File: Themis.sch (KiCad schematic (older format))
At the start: 37 parts, among them J10 Conn_01x01, J11 Conn_01x01, J12 Conn_01x01, J13 Conn_01x01, J17 SMA, J18 Conn_01x01, J20 Conn_01x01, J5 Conn_01x05, J7 SMA, J8 SMA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

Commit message: preparing themis v2
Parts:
- D5, D6: renamed from D?; footprint (none) -> Diode_SMD:D_SMB_Handsoldering
- J17, J8: footprint SMA_PINS:SMA_EDGE_NRW -> SMA_PINS:SMA_PINS
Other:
- note added: "V2.0\n\n\n\n28B0570-000\n28B0562-100\nlaird"
- note added: "att 30dB or less\ndepending on your \noutput p0wa\n"
- note removed: "28B0562-100\nlaird"
- note removed: "att 30dB\n"
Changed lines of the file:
@@
 	6100 3800 6150 3800
 Connection ~ 6150 3800
-Text Notes 3700 3650 0    60   ~ 0
-att 30dB\n
+Text Notes 3650 3550 0    60   ~ 0
+att 30dB or less\ndepending on your \noutput p0wa\n
 $Comp
 L D_Small_ALT D1
@@
 $EndComp
 $Comp
-L GND #PWR023
+L GND #PWR022
 U 1 1 5A4D7C62
 P 5450 1350
-F 0 "#PWR023" H 5450 1100 50  0001 C CNN
+F 0 "#PWR022" H 5450 1100 50  0001 C CNN
 F 1 "GND" H 5450 1200 50  0000 C CNN
 F 2 "" H 5450 1350 50  0001 C CNN
@@
 	5450 1350 5450 1400
 $Comp
-L GND #PWR024
+L GND #PWR023
 U 1 1 5A4D84CD
 P 6800 5700
-F 0 "#PWR024" H 6800 5450 50  0001 C CNN
+F 0 "#PWR023" H 6800 5450 50  0001 C CNN
 F 1 "GND" H 6800 5550 50  0000 C CNN
 F 2 "" H 6800 5700 50  0001 C CNN
@@
 	6750 5700 6800 5700
 $Comp
-L GND #PWR025
+L GND #PWR024
 U 1 1 5A4D88D2
 P 5050 5700
-F 0 "#PWR025" H 5050 5450 50  0001 C CNN
+F 0 "#PWR024" H 5050 5450 50  0001 C CNN
 F 1 "GND" H 5050 5550 50  0000 C CNN
 F 2 "" H 5050 5700 50  0001 C CNN
@@
 	5100 5700 5050 5700
 $Comp
-L PWR_FLAG #FLG026
+L PWR_FLAG #FLG025
 U 1 1 5A4D8E5C
 P 10350 1100
-F 0 "#FLG026" H 10350 1175 50  0001 C CNN
+F 0 "#FLG025" H 10350 1175 50  0001 C CNN
 F 1 "PWR_FLAG" H 10350 1250 50  0000 C CNN
 F 2 "" H 10350 1100 50  0001 C CNN
@@
 F 0 "J8" H 6460 1770 50  0000 C CNN
 F 1 "SMA" V 6565 1650 50  0000 C CNN
-F 2 "SMA_PINS:SMA_EDGE_NRW" H 6450 1650 50  0001 C CNN
+F 2 "SMA_PINS:SMA_PINS" H 6450 1650 50  0001 C CNN
 F 3 "" H 6450 1650 50  0001 C CNN
 	1    6450 1650
@@
 $EndComp
 $Comp
-L GND #PWR029
+L GND #PWR026
 U 1 1 5A4DB06F
 P 5050 1900
-F 0 "#PWR029" H 5050 1650 50  0001 C CNN
+F 0 "#PWR026" H 5050 1650 50  0001 C CNN
 F 1 "GND" H 5050 1750 50  0000 C CNN
 F 2 "" H 5050 1900 50  0001 C CNN
@@
 $EndComp
 $Comp
-L GND #PWR030
+L GND #PWR027
 U 1 1 5A4DCFB7
 P 9600 1300
-F 0 "#PWR030" H 9600 1050 50  0001 C CNN
+F 0 "#PWR027" H 9600 1050 50  0001 C CNN
 F 1 "GND" H 9600 1150 50  0000 C CNN
 F 2 "" H 9600 1300 50  0001 C CNN
@@
 $EndComp
 $Comp
-L GND #PWR031
+L GND #PWR028
 U 1 1 5A4DD062
 P 9600 1150
-F 0 "#PWR031" H 9600 900 50  0001 C CNN
+F 0 "#PWR028" H 9600 900 50  0001 C CNN
 F 1 "GND" H 9600 1000 50  0000 C CNN
 F 2 "" H 9600 1150 50  0001 C CNN
@@
 $EndComp
 $Comp
-L GND #PWR032
+L GND #PWR029
 U 1 1 5A4DD0B9
 P 9600 1000
-F 0 "#PWR032" H 9600 750 50  0001 C CNN
+F 0 "#PWR029" H 9600 750 50  0001 C CNN
 F 1 "GND" H 9600 850 50  0000 C CNN
 F 2 "" H 9600 1000 50  0001 C CNN
@@
 $EndComp
 $Comp
-L GND #PWR033
+L GND #PWR030
 U 1 1 5A4DD0C6
 P 9600 850
-F 0 "#PWR033" H 9600 600 50  0001 C CNN
+F 0 "#PWR030" H 9600 600 50  0001 C CNN
 F 1 "GND" H 9600 700 50  0000 C CNN
 F 2 "" H 9600 850 50  0001 C CNN
@@
 	9650 850  9600 850
 $Comp
-L GND #PWR035
+L GND #PWR031
 U 1 1 5A4DE381
 P 3500 4200
-F 0 "#PWR035" H 3500 3950 50  0001 C CNN
+F 0 "#PWR031" H 3500 3950 50  0001 C CNN
 F 1 "GND" H 3500 4050 50  0000 C CNN
 F 2 "" H 3500 4200 50  0001 C CNN
@@
 F 0 "J17" H 3260 4320 50  0000 C CNN
 F 1 "SMA" V 3365 4200 50  0000 C CNN
-F 2 "SMA_PINS:SMA_EDGE_NRW" H 3250 4200 50  0001 C CNN
+F 2 "SMA_PINS:SMA_PINS" H 3250 4200 50  0001 C CNN
 F 3 "" H 3250 4200 50  0001 C CNN
 	1    3250 4200
@@
 $EndComp
 $Comp
-L GND #PWR037
+L GND #PWR032
 U 1 1 5A4E5F01
 P 9600 1750
-F 0 "#PWR037" H 9600 1500 50  0001 C CNN
+F 0 "#PWR032" H 9600 1500 50  0001 C CNN
 F 1 "GND" H 9600 1600 50  0000 C CNN
 F 2 "" H 9600 1750 50  0001 C CNN
@@
 $EndComp
 $Comp
-L GND #PWR038
+L GND #PWR033
 U 1 1 5A4E5F1B
 P 9600 1550
-F 0 "#PWR038" H 9600 1300 50  0001 C CNN
+F 0 "#PWR033" H 9600 1300 50  0001 C CNN
 F 1 "GND" H 9600 1400 50  0000 C CNN
 F 2 "" H 9600 1550 50  0001 C CNN
@@
 	9650 1550 9600 1550
 Text Notes 8100 1550 0    60   ~ 0
-28B0562-100\nlaird
+V2.0\n\n\n\n28B0570-000\n28B0562-100\nlaird
 Wire Wire Line
 	5300 2450 5300 3800
 NoConn ~ 6100 6150
 $Comp
-L D_Zener D?
+L D_Zener D5
 U 1 1 5B4B9FE5
 P 6650 5950
-F 0 "D?" H 6650 6050 50  0000 C CNN
+F 0 "D5" H 6650 6050 50  0000 C CNN
 F 1 "BZX84C3V3LT116" H 6650 5850 50  0000 C CNN
-F 2 "" H 6650 5950 50  0001 C CNN
+F 2 "Diode_SMD:D_SMB_Handsoldering" H 6650 5950 50  0001 C CNN
 F 3 "" H 6650 5950 50  0001 C CNN
 	1    6650 5950
@@
 $EndComp
 $Comp
-L D_Zener D?
+L D_Zener D6
 U 1 1 5B4BA0A6
 P 5200 6150
-F 0 "D?" H 5250 6050 50  0000 C CNN
+F 0 "D6" H 5250 6050 50  0000 C CNN
 F 1 "BZX84C3V3LT116" H 5250 6300 50  0000 C CNN
-F 2 "" H 5200 6150 50  0001 C CNN
+F 2 "Diode_SMD:D_SMB_Handsoldering" H 5200 6150 50  0001 C CNN
 F 3 "" H 5200 6150 50  0001 C CNN
 	1    5200 6150
@@
 $EndComp
 $Comp
-L GND #PWR?
+L GND #PWR034
 U 1 1 5B4BA198
 P 5000 6150
-F 0 "#PWR?" H 5000 5900 50  0001 C CNN
+F 0 "#PWR034" H 5000 5900 50  0001 C CNN
 F 1 "GND" H 5000 6000 50  0000 C CNN
 F 2 "" H 5000 6150 50  0001 C CNN
@@
 	5050 6150 5000 6150
 $Comp
-L GND #PWR?
+L GND #PWR035
 U 1 1 5B4BA291
 P 6850 5950
-F 0 "#PWR?" H 6850 5700 50  0001 C CNN
+F 0 "#PWR035" H 6850 5700 50  0001 C CNN
 F 1 "GND" H 6850 5800 50  0000 C CNN
 F 2 "" H 6850 5950 50  0001 C CNN

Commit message: Themis V2
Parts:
- removed D5, D6: BZX84C3V3LT116, Diode_SMD:D_SMB_Handsoldering, symbol D_Zener
- U1: footprint Housings_SOIC:SOIC-8_3.9x4.9mm_Pitch1.27mm -> Package_SO:SOIC-8_3.9x4.9mm_P1.27mm
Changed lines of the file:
@@
 F 0 "U1" H 6500 5300 50  0000 L CNN
 F 1 "LMC6482" H 6500 4900 50  0000 L CNN
-F 2 "Housings_SOIC:SOIC-8_3.9x4.9mm_Pitch1.27mm" H 6500 5100 50  0001 C CNN
+F 2 "Package_SO:SOIC-8_3.9x4.9mm_P1.27mm" H 6500 5100 50  0001 C CNN
 F 3 "" H 6500 5100 50  0001 C CNN
 	2    6500 5100
@@
 F 0 "U1" H 5350 5300 50  0000 L CNN
 F 1 "LMC6482" H 5350 4900 50  0000 L CNN
-F 2 "Housings_SOIC:SOIC-8_3.9x4.9mm_Pitch1.27mm" H 5350 5100 50  0001 C CNN
+F 2 "Package_SO:SOIC-8_3.9x4.9mm_P1.27mm" H 5350 5100 50  0001 C CNN
 F 3 "" H 5350 5100 50  0001 C CNN
 	1    5350 5100
@@
 Wire Wire Line
 	5350 5400 5350 5450
-Wire Wire Line
-	5350 5650 5350 6150
 $Comp
 L C_Small C2
@@
 FWD\n
 Wire Wire Line
-	5350 6150 5700 6150
-Wire Wire Line
 	5800 6150 5800 5950
 Wire Wire Line
@@
 Text Notes 5950 5950 0    60   ~ 0
 Refl\n
-Text Notes 5550 6100 2    60   ~ 0
-FWD\n
 $Comp
 L Conn_01x01 J20
@@
 	5300 2450 5300 3800
 NoConn ~ 6100 6150
-$Comp
-L D_Zener D5
-U 1 1 5B4B9FE5
-P 6650 5950
-F 0 "D5" H 6650 6050 50  0000 C CNN
-F 1 "BZX84C3V3LT116" H 6650 5850 50  0000 C CNN
-F 2 "Diode_SMD:D_SMB_Handsoldering" H 6650 5950 50  0001 C CNN
-F 3 "" H 6650 5950 50  0001 C CNN
-	1    6650 5950
-	1    0    0    -1
-$EndComp
-$Comp
-L D_Zener D6
-U 1 1 5B4BA0A6
-P 5200 6150
-F 0 "D6" H 5250 6050 50  0000 C CNN
-F 1 "BZX84C3V3LT116" H 5250 6300 50  0000 C CNN
-F 2 "Diode_SMD:D_SMB_Handsoldering" H 5200 6150 50  0001 C CNN
-F 3 "" H 5200 6150 50  0001 C CNN
-	1    5200 6150
-	-1   0    0    1
-$EndComp
-$Comp
-L GND #PWR034
-U 1 1 5B4BA198
-P 5000 6150
-F 0 "#PWR034" H 5000 5900 50  0001 C CNN
-F 1 "GND" H 5000 6000 50  0000 C CNN
-F 2 "" H 5000 6150 50  0001 C CNN
-F 3 "" H 5000 6150 50  0001 C CNN
-	1    5000 6150
-	0    1    1    0
-$EndComp
-Wire Wire Line
-	5050 6150 5000 6150
-$Comp
-L GND #PWR035
-U 1 1 5B4BA291
-P 6850 5950
-F 0 "#PWR035" H 6850 5700 50  0001 C CNN
-F 1 "GND" H 6850 5800 50  0000 C CNN
-F 2 "" H 6850 5950 50  0001 C CNN
-F 3 "" H 6850 5950 50  0001 C CNN
-	1    6850 5950
-	0    -1   -1   0
-$EndComp
-Wire Wire Line
-	6800 5950 6850 5950
 Connection ~ 5300 3800
 Wire Wire Line
 	6100 2750 6100 3000
+Text Notes 5550 6100 2    60   ~ 0
+FWD\n
+Wire Wire Line
+	5350 6150 5700 6150
+Wire Wire Line
+	5350 5650 5350 6150
 $EndSCHEMATC

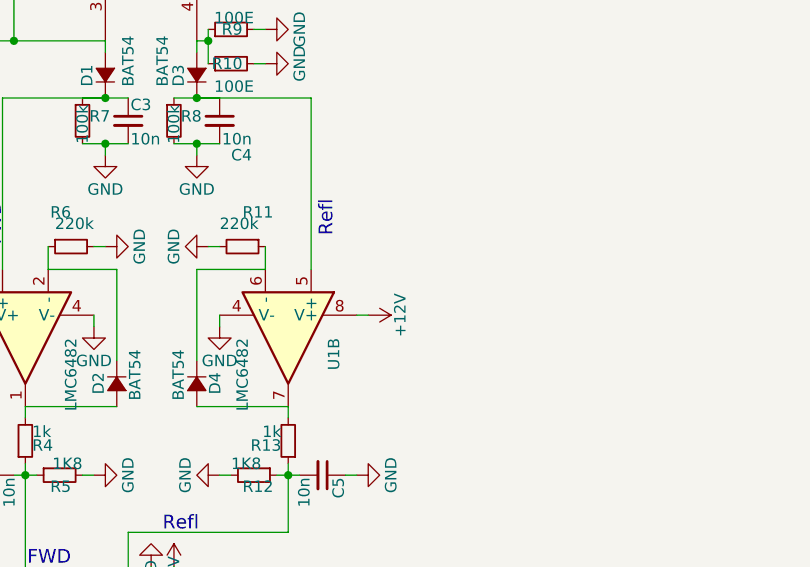
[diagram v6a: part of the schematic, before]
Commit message: decoupling cap added in the op-amp power rail
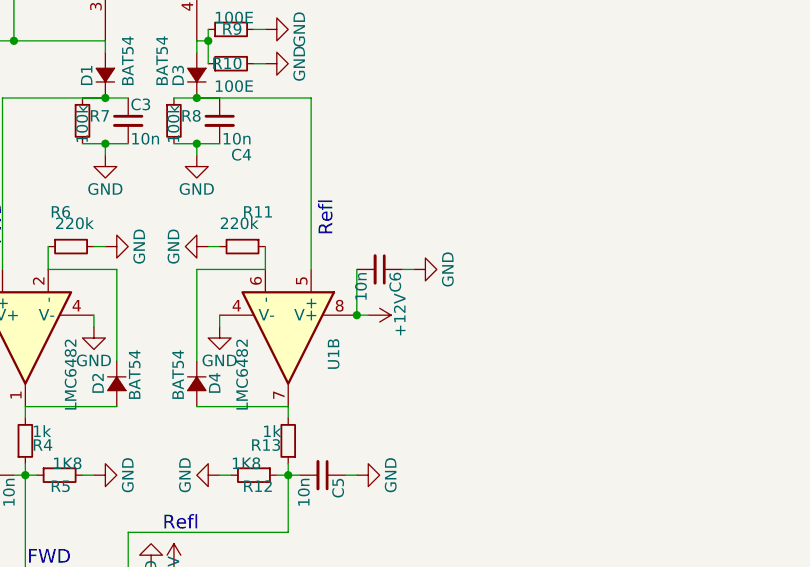
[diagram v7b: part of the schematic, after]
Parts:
- added C6: 10n, Capacitor_SMD:C_1206_3216Metric_Pad1.24x1.80mm_HandSolder, symbol C_Small
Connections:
- net +12V: now also C6.2
- net GND: now also C6.1
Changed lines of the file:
@@
 Wire Wire Line
 	5350 5650 5350 6150
+$Comp
+L C_Small C6
+U 1 1 5B56C377
+P 6900 4800
+F 0 "C6" H 6910 4870 50  0000 L CNN
+F 1 "10n" H 6910 4720 50  0000 L CNN
+F 2 "Capacitor_SMD:C_1206_3216Metric_Pad1.24x1.80mm_HandSolder" H 6900 4800 50  0001 C CNN
+F 3 "" H 6900 4800 50  0001 C CNN
+	1    6900 4800
+	0    1    1    0
+$EndComp
+$Comp
+L GND #PWR034
+U 1 1 5B56C37D
+P 7050 4800
+F 0 "#PWR034" H 7050 4550 50  0001 C CNN
+F 1 "GND" H 7050 4650 50  0000 C CNN
+F 2 "" H 7050 4800 50  0001 C CNN
+F 3 "" H 7050 4800 50  0001 C CNN
+	1    7050 4800
+	0    -1   -1   0
+$EndComp
+Wire Wire Line
+	7000 4800 7050 4800
+Wire Wire Line
+	6800 5000 6800 4800
+Connection ~ 6800 5000
 $EndSCHEMATC
